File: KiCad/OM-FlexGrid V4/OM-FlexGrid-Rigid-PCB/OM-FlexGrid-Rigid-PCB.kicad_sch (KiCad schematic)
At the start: 62 parts, among them IC1 ICM-42688-P, J1 Conn_01x06_Pin, J2 BAT Terminal, J3 Conn_01x20, J4 USB_C_Receptacle, J5 Conn_01x02, J6 Conn_01x03_Pin, J7 Conn_01x02_Pin, J9 Micro_SD_Card, Q1 IRLML2060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

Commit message: V4 rev: ADC matrix caps 2.2uF -> 100pF, MAX16054 footprint TSOT-23-6
Two real design changes applied to the V4 Rigid PCB this revision:

1. ADC matrix-row caps C12, C13, C14, C15 changed from 2.2 uF
   to 100 pF. This is Option 3 from the README's "Known carry-forward
   concerns" section. New LCSC: C14858 (100 pF 0603, Basic tier).
   RC time constant with the 10 kohm row pulldown drops from ~22 ms
   to ~1 us, well below the per-column ADC dwell time. Resolves the
   column-to-column bleed problem V3 saw with the 2.2 uF parts
   without sacrificing high-frequency noise filtering.

2. MAX1 (MAX16054 soft-power controller) footprint swapped from
   SOT-23-6 to TSOT-23-6. The LCSC part C79401 is actually
   MAX16054AZT+T which ships in TSOT-23-6. Pads are pad-compatible
   between SOT-23-6 and TSOT-23-6 (same pitch, same outline,
   thinner profile), so a part placed on the old footprint would
   have worked, but matching the schematic footprint to the actual
   package on disk is cleaner for downstream KiCad consumers.

3. Side change: MAX1's schematic value cleaned up from "~" to
   "MAX16054" so the BOM and silkscreen identify it properly.

Regenerated fab files in jlcpcb/ to reflect all three changes:
- gerber files updated
- BOM-OM-FlexGrid-Rigid-PCB.csv shows C12-C15 = 100 pF / C14858
- BOM also shows MAX1 / MAX16054 / TSOT-23-6
- CPL-OM-FlexGrid-Rigid-PCB.csv positions consistent

KiCad backups from the design session included in the commit.
V3 working-tree edits remain untouched.

Co-Authored-By: turfptax-claude O4.7 <turfptax-claude@openmuscle.org>
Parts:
- C12, C13, C14, C15: value 2.2 uF -> 100 pF
- C9: LCSC C12530 -> C100082
- D4: footprint Diode_SMD:D_SOD-123F -> Diode_SMD:D_SOD-123; LCSC (none) -> C22440662
- D5: LCSC (none) -> C2827305
- MAX1: value (none) -> MAX16054; footprint Package_TO_SOT_SMD:SOT-23-6 -> Package_TO_SOT_SMD:TSOT-23-6
- R10, R11: LCSC C25744 -> C25804
- R16, R17, R18: LCSC C25804 -> C23138
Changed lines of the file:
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@@
 		(in_pos_files yes)
 		(dnp no)
-		(fields_autoplaced yes)
 		(property "Reference" "MAX1"
 			(at 125.3841 147.32 0)
@@
 			)
 		)
-		(property "Value" ""
-			(at 123.19 152.4 0)
+		(property "Value" "MAX16054"
+			(at 112.776 146.304 0)
 			(show_name no)
 			(do_not_autoplace no)
@@
 			)
 		)
-		(property "Footprint" "Package_TO_SOT_SMD:SOT-23-6"
+		(property "Footprint" "Package_TO_SOT_SMD:TSOT-23-6"
 			(at 123.19 152.4 0)
 			(hide yes)
@@
 			)
 		)
-		(property "Footprint" "Diode_SMD:D_SOD-123F"
+		(property "Footprint" "Diode_SMD:D_SOD-123"
 			(at 27.305 161.29 0)
 			(hide yes)
@@
 			)
 		)
+		(property "LCSC" "C22440662"
+			(at 34.29 160.02 0)
+			(hide yes)
+			(show_name no)
+			(do_not_autoplace no)
+			(effects
+				(font
+					(size 1.27 1.27)
+				)
+			)
+		)
 		(pin "1"
 		)
@@
 			)
 		)
+		(property "LCSC" "C2827305"
+			(at 180.34 20.32 0)
+			(hide yes)
+			(show_name no)
+			(do_not_autoplace no)
+			(effects
+				(font
+					(size 1.27 1.27)
+				)
+			)
+		)
 		(pin "6"
 		)
@@
 			)
 		)
-		(property "Value" "2.2 uF"
+		(property "Value" "100 pF"
 			(at 114.681 69.723 0)
 			(hide yes)
@@
 			)
 		)
-		(property "LCSC" "C25744"
+		(property "LCSC" "C25804"
 			(at 46.8884 175.768 0)
 			(hide yes)
@@
 			)
 		)
-		(property "LCSC" "C25804"
+		(property "LCSC" "C23138"
 			(at 190.754 29.21 0)
 			(hide yes)
@@
 			)
 		)
-		(property "Value" "2.2 uF"
+		(property "Value" "100 pF"
 			(at 104.521 69.723 0)
 			(hide yes)
@@
 			)
 		)
-		(property "Value" "2.2 uF"
+		(property "Value" "100 pF"
 			(at 109.601 69.723 0)
 			(hide yes)
@@
 			)
 		)
-		(property "LCSC" "C25804"
+		(property "LCSC" "C23138"
 			(at 190.754 39.37 0)
 			(hide yes)
@@
 			)
 		)
-		(property "LCSC" "C25744"
+		(property "LCSC" "C25804"
 			(at 47.752 184.0484 0)
 			(hide yes)
@@
 			)
 		)
-		(property "Value" "2.2 uF"
+		(property "Value" "100 pF"
 			(at 99.441 69.723 0)
 			(hide yes)
@@
 			)
 		)
-		(property "LCSC" "C25804"
+		(property "LCSC" "C23138"
 			(at 190.754 34.29 0)
 			(hide yes)
@@
 			)
 		)
-		(property "LCSC" "C12530"
+		(property "LCSC" "C100082"
 			(at 47.371 160.1216 0)
 			(hide yes)

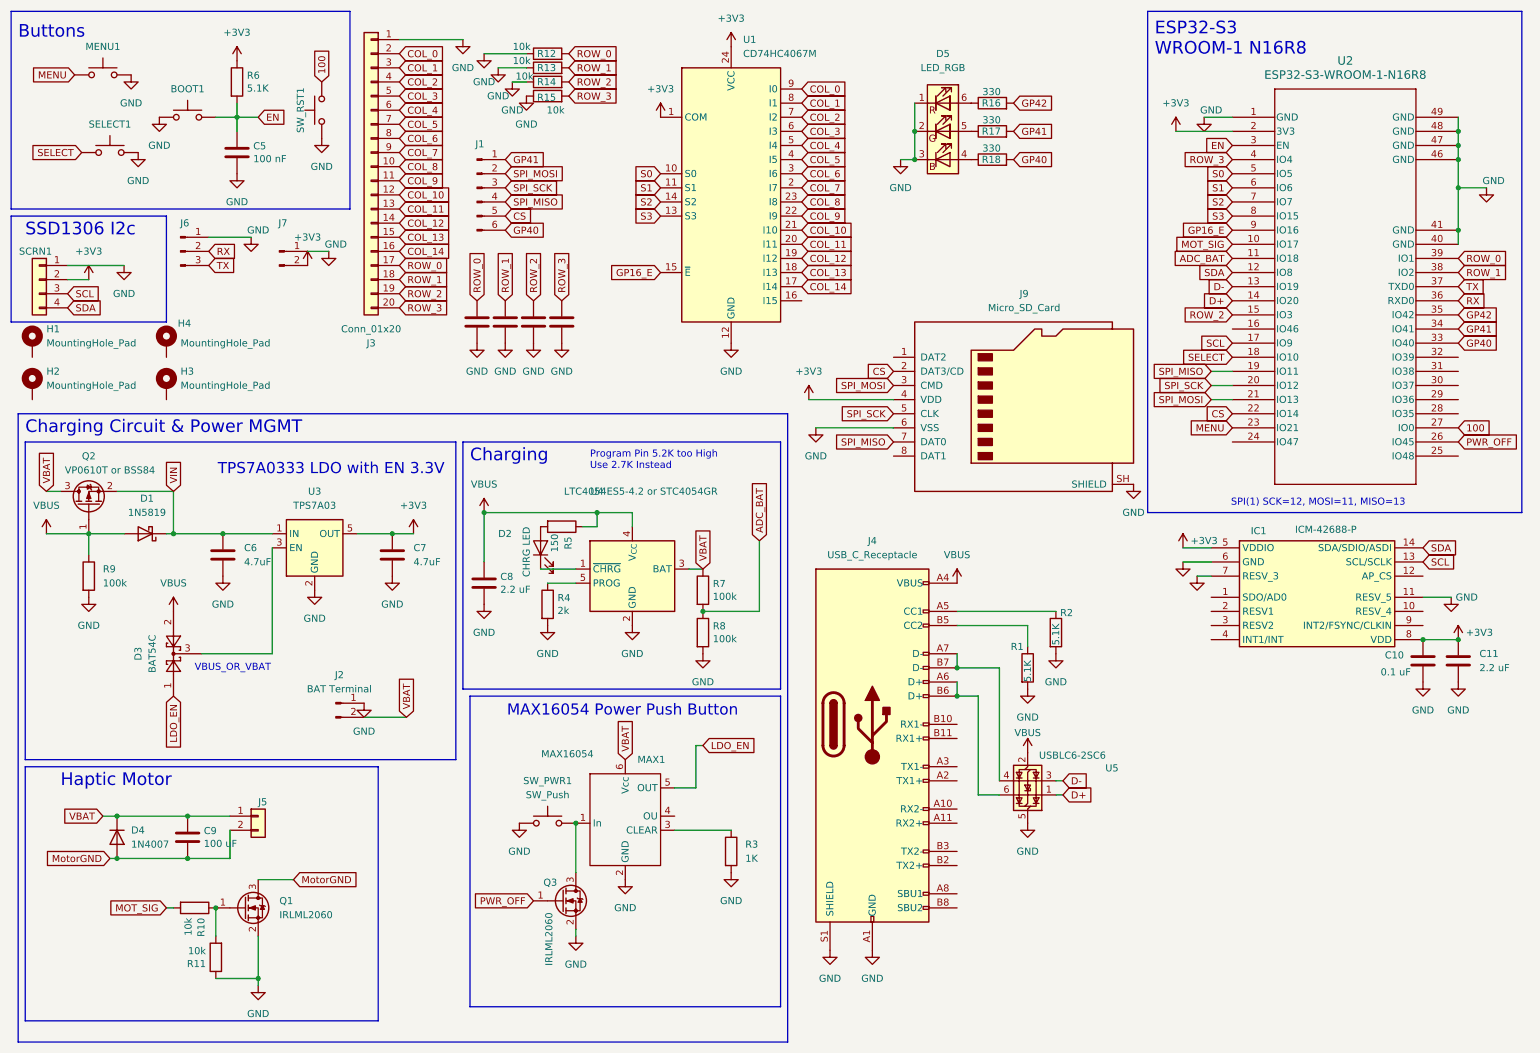
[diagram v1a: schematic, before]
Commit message: Add FlexGrid V4 design with onboard SD card; clean up backups
V4 rigid and flex PCB design. Adds an onboard microSD card so the band can log capture sessions standalone, without a tethered PC. V4 3D and animation assets (Blender, glTF, STEP) are tracked via Git LFS.

Also stop versioning KiCad and Blender auto-backups (*-backups/, *.blend[0-9]) and remove the old backup archives.

Suggested-by: Kyle.T.Y <64039282+HeatRIderHR@users.noreply.github.com>
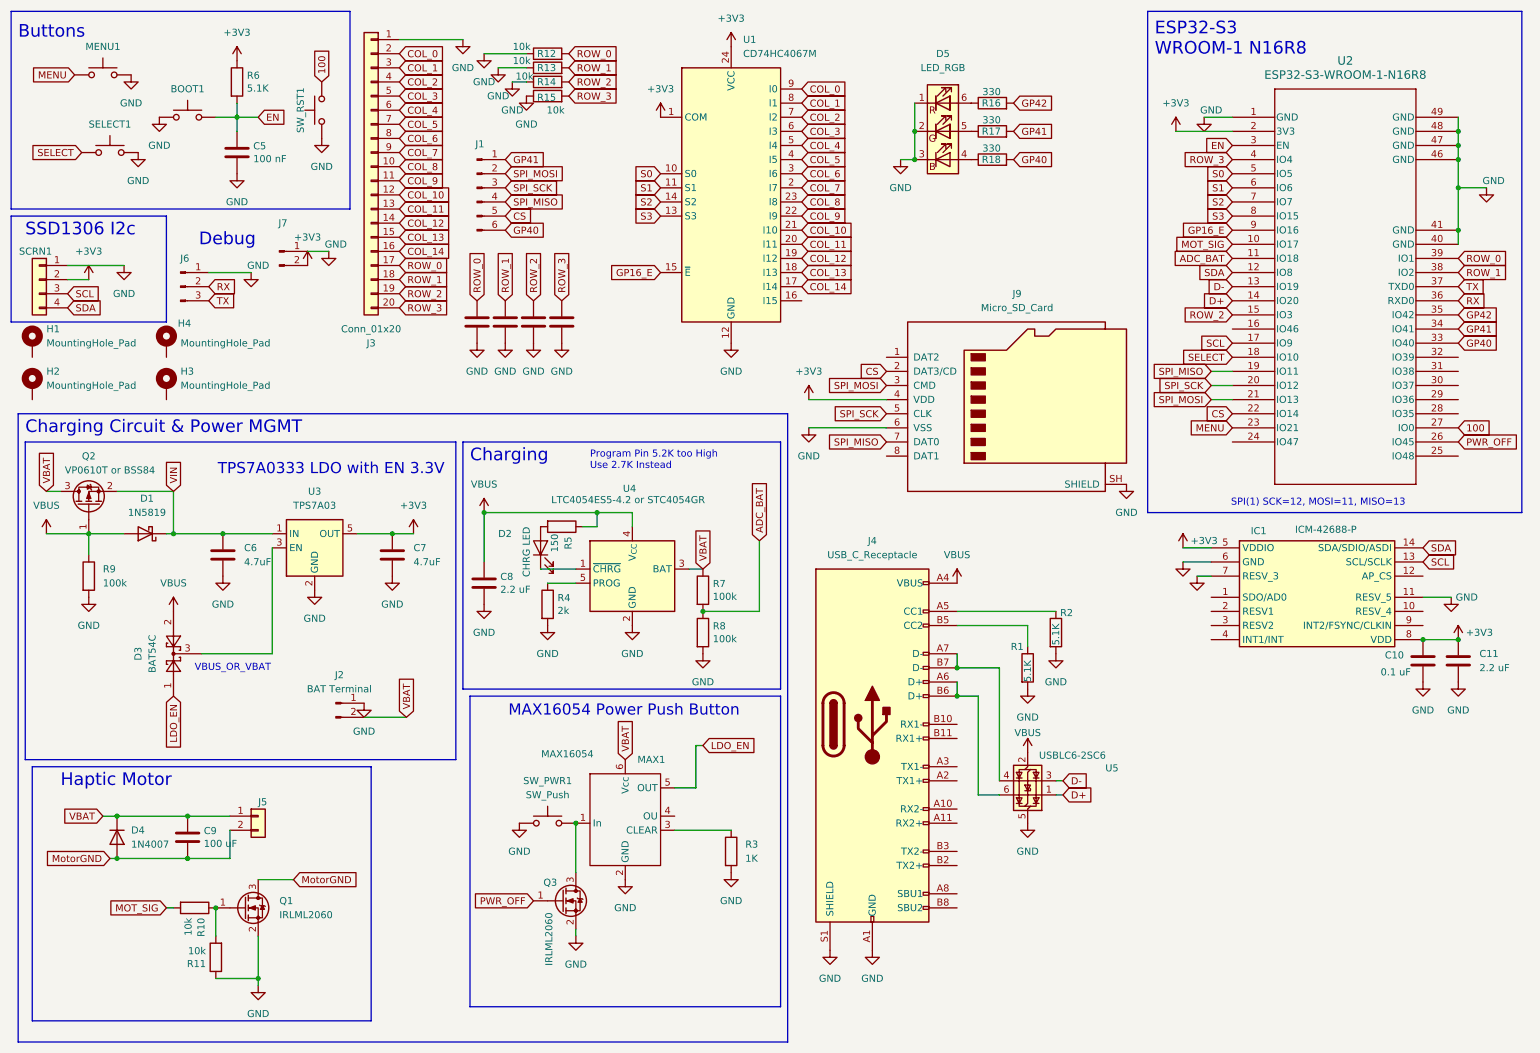
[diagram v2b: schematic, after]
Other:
- note added: "Debug"
- moved on the sheet: J6, J9
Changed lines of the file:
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@@
 	)
 	(rectangle
-		(start 15.24 148.59)
-		(end 78.74 194.31)
+		(start 16.51 148.59)
+		(end 77.47 194.31)
 		(stroke
 			(width 0)
@@
 	(text "MAX16054 Power Push Button"
 		(exclude_from_sim no)
-		(at 143.51 139.7 0)
+		(at 143.764 139.7 0)
 		(effects
 			(font
@@
 		)
 	)
+	(text "Debug"
+		(exclude_from_sim no)
+		(at 46.482 55.118 0)
+		(effects
+			(font
+				(size 2.27 2.27)
+			)
+			(justify left bottom)
+		)
+	)
 	(junction
 		(at 273.05 39.37)
@@
 	(wire
 		(pts
-			(xy 157.48 87.63) (xy 171.45 87.63)
+			(xy 156.21 87.63) (xy 170.18 87.63)
 		)
 		(stroke
@@
 	(wire
 		(pts
-			(xy 55.88 53.34) (xy 48.26 53.34)
+			(xy 55.88 59.69) (xy 48.26 59.69)
 		)
 		(stroke
@@
 	(wire
 		(pts
-			(xy 156.21 82.55) (xy 171.45 82.55)
+			(xy 156.21 82.55) (xy 170.18 82.55)
 		)
 		(stroke
@@
 	(global_label "CS"
 		(shape input)
-		(at 171.45 77.47 180)
+		(at 170.18 77.47 180)
 		(fields_autoplaced yes)
 		(effects
@@
 		)
 		(property "Intersheetrefs" "${INTERSHEET_REFS}"
-			(at 165.9853 77.47 0)
+			(at 164.7153 77.47 0)
 			(hide yes)
 			(show_name no)
@@
 	(global_label "RX"
 		(shape input)
-		(at 48.26 55.88 0)
+		(at 48.26 62.23 0)
 		(fields_autoplaced yes)
 		(effects
@@
 		)
 		(property "Intersheetrefs" "${INTERSHEET_REFS}"
-			(at 53.7247 55.88 0)
+			(at 53.7247 62.23 0)
 			(hide yes)
 			(show_name no)
@@
 	(global_label "SPI_SCK"
 		(shape input)
-		(at 171.45 85.09 180)
+		(at 170.18 85.09 180)
 		(fields_autoplaced yes)
 		(effects
@@
 		)
 		(property "Intersheetrefs" "${INTERSHEET_REFS}"
-			(at 160.6634 85.09 0)
+			(at 159.3934 85.09 0)
 			(hide yes)
 			(show_name no)
@@
 	(global_label "SPI_MOSI"
 		(shape input)
-		(at 171.45 80.01 180)
+		(at 170.18 80.01 180)
 		(fields_autoplaced yes)
 		(effects
@@
 		)
 		(property "Intersheetrefs" "${INTERSHEET_REFS}"
-			(at 159.8167 80.01 0)
+			(at 158.5467 80.01 0)
 			(hide yes)
 			(show_name no)
@@
 	(global_label "SPI_MISO"
 		(shape input)
-		(at 171.45 90.17 180)
+		(at 170.18 90.17 180)
 		(fields_autoplaced yes)
 		(effects
@@
 		)
 		(property "Intersheetrefs" "${INTERSHEET_REFS}"
-			(at 159.8167 90.17 0)
+			(at 158.5467 90.17 0)
 			(hide yes)
 			(show_name no)
@@
 	(global_label "TX"
 		(shape input)
-		(at 48.26 58.42 0)
+		(at 48.26 64.77 0)
 		(fields_autoplaced yes)
 		(effects
@@
 		)
 		(property "Intersheetrefs" "${INTERSHEET_REFS}"
-			(at 53.4223 58.42 0)
+			(at 53.4223 64.77 0)
 			(hide yes)
 			(show_name no)
@@
 	(symbol
 		(lib_id "power:GND")
-		(at 214.63 97.79 0)
+		(at 213.36 97.79 0)
 		(unit 1)
 		(body_style 1)
@@
 		(fields_autoplaced yes)
 		(property "Reference" "#PWR020"
-			(at 214.63 104.14 0)
+			(at 213.36 104.14 0)
 			(hide yes)
 			(show_name no)
@@
 		)
 		(property "Value" "GND"
-			(at 214.63 102.87 0)
+			(at 213.36 102.87 0)
 			(show_name no)
 			(do_not_autoplace no)
@@
 		)
 		(property "Footprint" ""
-			(at 214.63 97.79 0)
+			(at 213.36 97.79 0)
 			(hide yes)
 			(show_name no)
@@
 		)
 		(property "Datasheet" ""
-			(at 214.63 97.79 0)
+			(at 213.36 97.79 0)
 			(hide yes)
 			(show_name no)
@@
 		)
 		(property "Description" "Power symbol creates a global label with name \"GND\" , ground"
-			(at 214.63 97.79 0)
+			(at 213.36 97.79 0)
 			(hide yes)
 			(show_name no)
@@
 	(symbol
 		(lib_id "power:GND")
-		(at 157.48 87.63 0)
+		(at 156.21 87.63 0)
 		(unit 1)
 		(body_style 1)
@@
 		(fields_autoplaced yes)
 		(property "Reference" "#PWR021"
-			(at 157.48 93.98 0)
+			(at 156.21 93.98 0)
 			(hide yes)
 			(show_name no)
@@
 		)
 		(property "Value" "GND"
-			(at 157.48 92.71 0)
+			(at 156.21 92.71 0)
 			(show_name no)
 			(do_not_autoplace no)
@@
 		)
 		(property "Footprint" ""
-			(at 157.48 87.63 0)
+			(at 156.21 87.63 0)
 			(hide yes)
 			(show_name no)
@@
 		)
 		(property "Datasheet" ""
-			(at 157.48 87.63 0)
+			(at 156.21 87.63 0)
 			(hide yes)
 			(show_name no)
@@
 		)
 		(property "Description" "Power symbol creates a global label with name \"GND\" , ground"
-			(at 157.48 87.63 0)
+			(at 156.21 87.63 0)
 			(hide yes)
 			(show_name no)
@@
 		(dnp no)
 		(property "Reference" "U4"
-			(at 118.11 99.06 0)
+			(at 123.952 98.552 0)
 			(show_name no)
 			(do_not_autoplace no)
@@
 		)
 		(property "Value" "LTC4054ES5-4.2 or STC4054GR"
-			(at 125.984 99.06 0)
+			(at 123.698 100.584 0)
 			(show_name no)
 			(do_not_autoplace no)
@@
 	(symbol
 		(lib_id "power:GND")
-		(at 55.88 53.34 0)
+		(at 55.88 59.69 0)
 		(unit 1)
 		(body_style 1)
@@
 		(dnp no)
 		(property "Reference" "#PWR012"
-			(at 55.88 59.69 0)
+			(at 55.88 66.04 0)
 			(hide yes)
 			(show_name no)
@@
 		)
 		(property "Value" "GND"
-			(at 57.15 52.07 0)
+			(at 57.15 58.42 0)
 			(show_name no)
 			(do_not_autoplace no)
@@
 		)
 		(property "Footprint" ""
-			(at 55.88 53.34 0)
+			(at 55.88 59.69 0)
 			(hide yes)
 			(show_name no)
@@
 		)
 		(property "Datasheet" ""
-			(at 55.88 53.34 0)
+			(at 55.88 59.69 0)
 			(hide yes)
 			(show_name no)
@@
 		)
 		(property "Description" ""
-			(at 55.88 53.34 0)
+			(at 55.88 59.69 0)
 			(show_name no)
 			(do_not_autoplace no)
@@
 	(symbol
 		(lib_id "Connector:Conn_01x03_Pin")
-		(at 43.18 55.88 0)
+		(at 43.18 62.23 0)
 		(unit 1)
 		(body_style 1)
@@
 		(dnp no)
 		(property "Reference" "J6"
-			(at 43.942 50.8 0)
+			(at 43.942 57.15 0)
 			(show_name no)
 			(do_not_autoplace no)
@@
 		)
 		(property "Value" "Conn_01x03_Pin"
-			(at 43.815 50.8 0)
+			(at 43.815 57.15 0)
 			(hide yes)
 			(show_name no)
@@
 		)
 		(property "Footprint" "Connector_PinHeader_2.54mm:PinHeader_1x03_P2.54mm_Vertical"
-			(at 43.18 55.88 0)
+			(at 43.18 62.23 0)
 			(hide yes)
 			(show_name no)
@@
 		)
 		(property "Datasheet" ""
-			(at 43.18 55.88 0)
+			(at 43.18 62.23 0)
 			(hide yes)
 			(show_name no)
@@
 		)
 		(property "Description" "Generic connector, single row, 01x03, script generated"
-			(at 43.18 55.88 0)
+			(at 43.18 62.23 0)
 			(hide yes)
 			(show_name no)
@@
 	(symbol
 		(lib_id "Connector:Micro_SD_Card")
-		(at 194.31 82.55 0)
+		(at 193.04 82.55 0)
 		(unit 1)
 		(body_style 1)
@@
 		(fields_autoplaced yes)
 		(property "Reference" "J9"
-			(at 194.945 63.5 0)
+			(at 193.675 63.5 0)
 			(show_name no)
 			(do_not_autoplace no)
@@
 		)
 		(property "Value" "Micro_SD_Card"
-			(at 194.945 66.04 0)
+			(at 193.675 66.04 0)
 			(show_name no)
 			(do_not_autoplace no)
@@
 		)
 		(property "Footprint" "footprints:CONN_503398-1892_MOL"
-			(at 223.52 74.93 0)
+			(at 222.25 74.93 0)
 			(hide yes)
 			(show_name no)
@@
 		)
 		(property "Datasheet" "https://www.we-online.com/components/products/datasheet/693072010801.pdf"
-			(at 194.31 82.55 0)
+			(at 193.04 82.55 0)
 			(hide yes)
 			(show_name no)
@@
 		)
 		(property "Description" "Micro SD Card Socket"
-			(at 194.31 82.55 0)
+			(at 193.04 82.55 0)
 			(hide yes)
 			(show_name no)

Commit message: V4 Rigid PCB: fix USBLC6 pinout + expand JLC-assembled BOM
USBLC6 ESD chip fix
-------------------
Swap the VBUS and GND power-flag connections on the USBLC6-2SC6
footprint in the schematic. Earlier revision wired pin 2 to VBUS
and pin 5 to GND, but the actual chip pinout is pin 2 = GND and
pin 5 = VCC. Result on the first populated V4 board was that the
USB enumerated VBUS (Windows chime) but the data lines were
clamped to garbage by the now-forward-biased internal ESD diodes,
so no COM port was assigned and esptool could not sync.

Workaround on the first board was to rotate the USBLC6 180 degrees
during placement (SOT-23-6 footprint is symmetric, so the I/O pin
pairs route correctly either way; only VCC/GND end up reversed).
This commit puts the corrected pinout into the schematic so the
next fab order from anyone (including community members pulling
from GitHub) gets a board that works without manual rework.

PCB regenerated against the new schematic. All gerbers, drill
files, BOM, and CPL are refreshed accordingly. GERBER zip in
jlcpcb/production_files/ is the as-ready-to-upload archive.

BOM expansion
-------------
While re-running the JLCPCB plugin, additional designators were
toggled to BOM-ON for JLC assembly (previously hand-solder):
  - C9 (100uF cap)
  - R10, R11 (10k pulldowns)
  - Q1 (IRLML2060)
  - J1 (programming header)
  - J7 (pin socket)
That reduces the hand-solder workload from earlier V4 plan; the
remaining hand-solder items are still the ESP32 module, mux,
microSD socket, USB-C, and Wurth FFC connector. Update the
README hand-solder list before the next bring-up if these counts
matter to anyone following along.

3D models
---------
Adds WRL export and an updated Blender file for the V4 board
revision so the mechanical fit-check renders match the corrected
layout. FlexGridV5.blend has been touched alongside as well
(no V4 functional implication).

Production output folder
------------------------
Adds a parallel production/ folder generated by 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
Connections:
- net D+: now also U5.4 (I/O2); no longer U5.1 (I/O1)
- net D-: now also U5.6 (I/O1); no longer U5.3 (I/O2)
- net GND: now also U5.2 (GND); no longer U5.5 (VBUS)
- net VBUS: now also U5.5 (VBUS); no longer U5.2 (GND)
- net at J4.A7 (D-), J4.B7 (D-): now also U5.1 (I/O1); no longer U5.4 (I/O2)
- net at J4.A6 (D+), J4.B6 (D+): now also U5.3 (I/O2); no longer U5.6 (I/O1)
